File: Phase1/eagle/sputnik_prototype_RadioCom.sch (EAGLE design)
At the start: 102 parts, among them Y1 32MHz

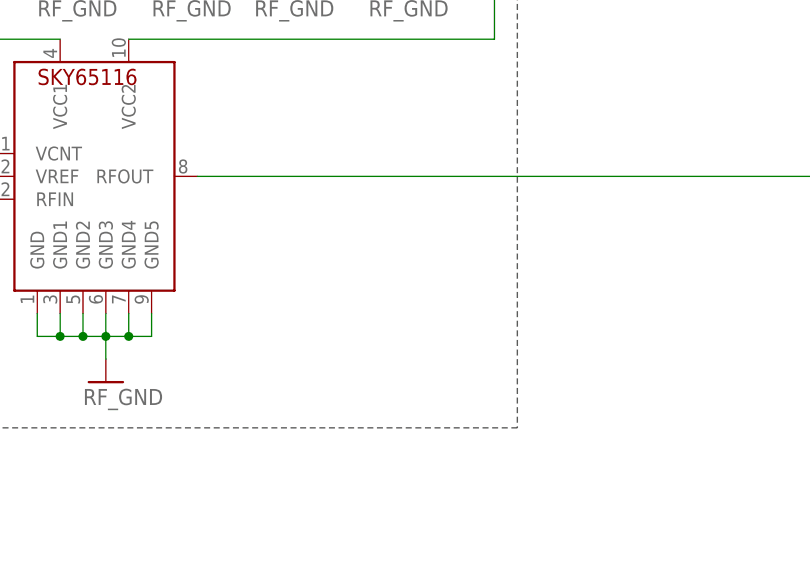
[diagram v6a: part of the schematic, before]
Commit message: Yep, that was a good idea. I added the other shield. And experimented with other layouts. Still needs a ton of work, but now it's going to be OK. OH CRAP the RXTX switch might have be wired the otherway: check this. That said, I think this is more sane. Power and nd caps need to be laid out, then signals.
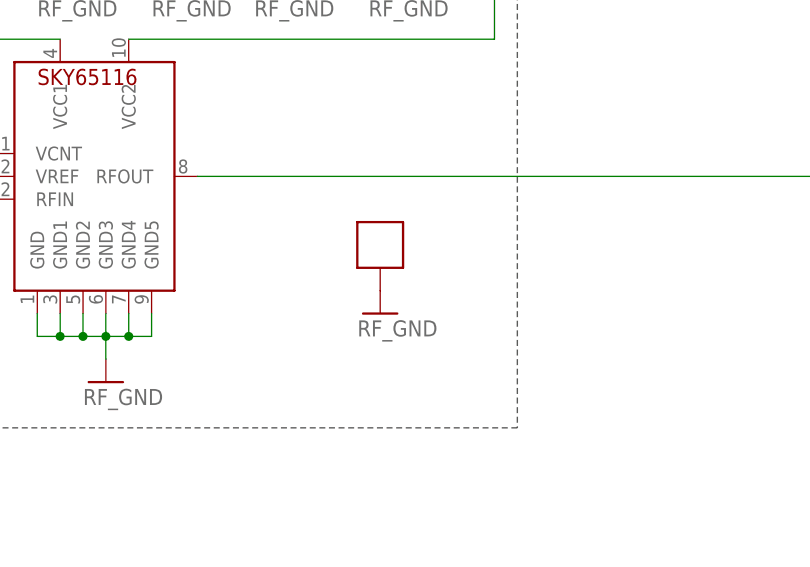
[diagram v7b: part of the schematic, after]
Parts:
- added SH2: BMI-S-202-SHIELD, hw-laird-bmi-s-202:BMI-S-202-SHIELD
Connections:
- net V+ renamed RIP
- net GND: now also SH2.P$1
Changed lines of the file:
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@@
 <part name="SH1" library="hw-laird-bmi-s-202" deviceset="BMI-S-202-SHIELD" device=""/>
 <part name="U$34" library="psas_c3_team05" deviceset="RF_GND" device=""/>
+<part name="SH2" library="hw-laird-bmi-s-202" deviceset="BMI-S-202-SHIELD" device=""/>
+<part name="U$36" library="psas_c3_team05" deviceset="RF_GND" device=""/>
 </parts>
 <sheets>
@@
 <instance part="SH1" gate="G$1" x="350.52" y="139.7"/>
 <instance part="U$34" gate="G$1" x="350.52" y="132.08"/>
+<instance part="SH2" gate="G$1" x="419.1" y="248.92"/>
+<instance part="U$36" gate="G$1" x="419.1" y="241.3"/>
 </instances>
 <busses>
@@
 <wire x1="170.18" y1="15.24" x2="170.18" y2="17.78" width="0.1524" layer="91"/>
 </segment>
+<segment>
+<pinref part="SH2" gate="G$1" pin="P$1"/>
+<pinref part="U$36" gate="G$1" pin="GND"/>
+</segment>
 </net>
-<net name="V+" class="0">
+<net name="RIP" class="0">
 <segment>
 <pinref part="TRSWITCH" gate="G$1" pin="VDD"/>

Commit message: Fixed symbol pins and locations
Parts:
- removed L7: (no value), rcl_custom:L-US0402-B-NOSILK
- added C44: 10nF, rcl_custom:C-EU0402-B-NOSILK
- C24: value 10nF -> 1nF
- L8: value 150nH -> 82nH
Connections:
- removed net N$24: L7.1, LNA.RFIN
- net GND: now also C44.2
- net LNA_IN: now also TRSWITCH.RF2; no longer TRSWITCH.RF3
- net N$2: now also TRSWITCH.RF3; no longer TRSWITCH.RF2
- net N$25: now also LNA.RFIN; no longer L7.2
- net VBIAS: now also C44.1
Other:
- note removed: "TODO: FIGURE OUT VALUE FOR L7"
- moved on the sheet: C24, C25, C43, L8
